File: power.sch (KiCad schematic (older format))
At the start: 34 parts, among them U1 TPS54325, U2 TPS54294

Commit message: Fix all the things
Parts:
- U1: symbol psu-components:TPS54325 -> Effect-Box-rescue:TPS54325-psu-components
- U2: symbol psu-components:TPS54294 -> Effect-Box-rescue:TPS54294-psu-components
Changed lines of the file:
@@
 $EndDescr
 $Comp
-L psu-components:TPS54325 U1
+L Effect-Box-rescue:TPS54325-psu-components U1
 U 1 1 5D81CBD0
 P 5700 2300
@@
 $EndComp
 $Comp
-L psu-components:TPS54294 U2
+L Effect-Box-rescue:TPS54294-psu-components U2
 U 1 1 5D821E10
 P 5750 4850

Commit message: Add PSU lib footprints
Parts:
- U1: symbol Effect-Box-rescue:TPS54325-psu-components -> Effect-Box-rescue:TPS54325
- U2: symbol Effect-Box-rescue:TPS54294-psu-components -> Effect-Box-rescue:TPS54294
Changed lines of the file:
@@
 $EndDescr
 $Comp
-L Effect-Box-rescue:TPS54325-psu-components U1
+L Effect-Box-rescue:TPS54325 U1
 U 1 1 5D81CBD0
 P 5700 2300
@@
 $EndComp
 $Comp
-L Effect-Box-rescue:TPS54294-psu-components U2
+L Effect-Box-rescue:TPS54294 U2
 U 1 1 5D821E10
 P 5750 4850

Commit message: Add footprints for real (such pain)
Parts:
- U1: footprint (none) -> Package_SO:TSSOP-14-1EP_4.4x5mm_P0.65mm
- U2: footprint (none) -> Package_SO:TSSOP-16-1EP_4.4x5mm_P0.65mm
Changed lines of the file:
@@
 F 0 "U1" H 5400 2700 50  0000 C CNN
 F 1 "TPS54325" H 5900 2700 50  0000 C CNN
-F 2 "" H 5700 2300 50  0001 C CNN
+F 2 "Package_SO:TSSOP-14-1EP_4.4x5mm_P0.65mm" H 5700 2300 50  0001 C CNN
 F 3 "" H 5700 2300 50  0001 C CNN
 	1    5700 2300
@@
 F 0 "U2" H 5450 5300 50  0000 C CNN
 F 1 "TPS54294" H 5950 5300 50  0000 C CNN
-F 2 "" H 5750 4850 50  0001 C CNN
+F 2 "Package_SO:TSSOP-16-1EP_4.4x5mm_P0.65mm" H 5750 4850 50  0001 C CNN
 F 3 "" H 5750 4850 50  0001 C CNN
 	1    5750 4850

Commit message: Export PSU components as libs
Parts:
- U1: symbol Effect-Box-rescue:TPS54325 -> tps54325:TPS54325
- U2: symbol Effect-Box-rescue:TPS54294 -> tps54294:TPS54294
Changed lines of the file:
@@
 $EndDescr
 $Comp
-L Effect-Box-rescue:TPS54325 U1
+L tps54325:TPS54325 U1
 U 1 1 5D81CBD0
 P 5700 2300
+AR Path="/5D81CBD0" Ref="U1"  Part="1"
+AR Path="/5D7D4441/5D81CBD0" Ref="U1"  Part="1"
 F 0 "U1" H 5400 2700 50  0000 C CNN
 F 1 "TPS54325" H 5900 2700 50  0000 C CNN
@@
 $EndComp
 $Comp
-L Effect-Box-rescue:TPS54294 U2
+L tps54294:TPS54294 U2
 U 1 1 5D821E10
 P 5750 4850
+AR Path="/5D821E10" Ref="U2"  Part="1"
+AR Path="/5D7D4441/5D821E10" Ref="U2"  Part="1"
 F 0 "U2" H 5450 5300 50  0000 C CNN
 F 1 "TPS54294" H 5950 5300 50  0000 C CNN

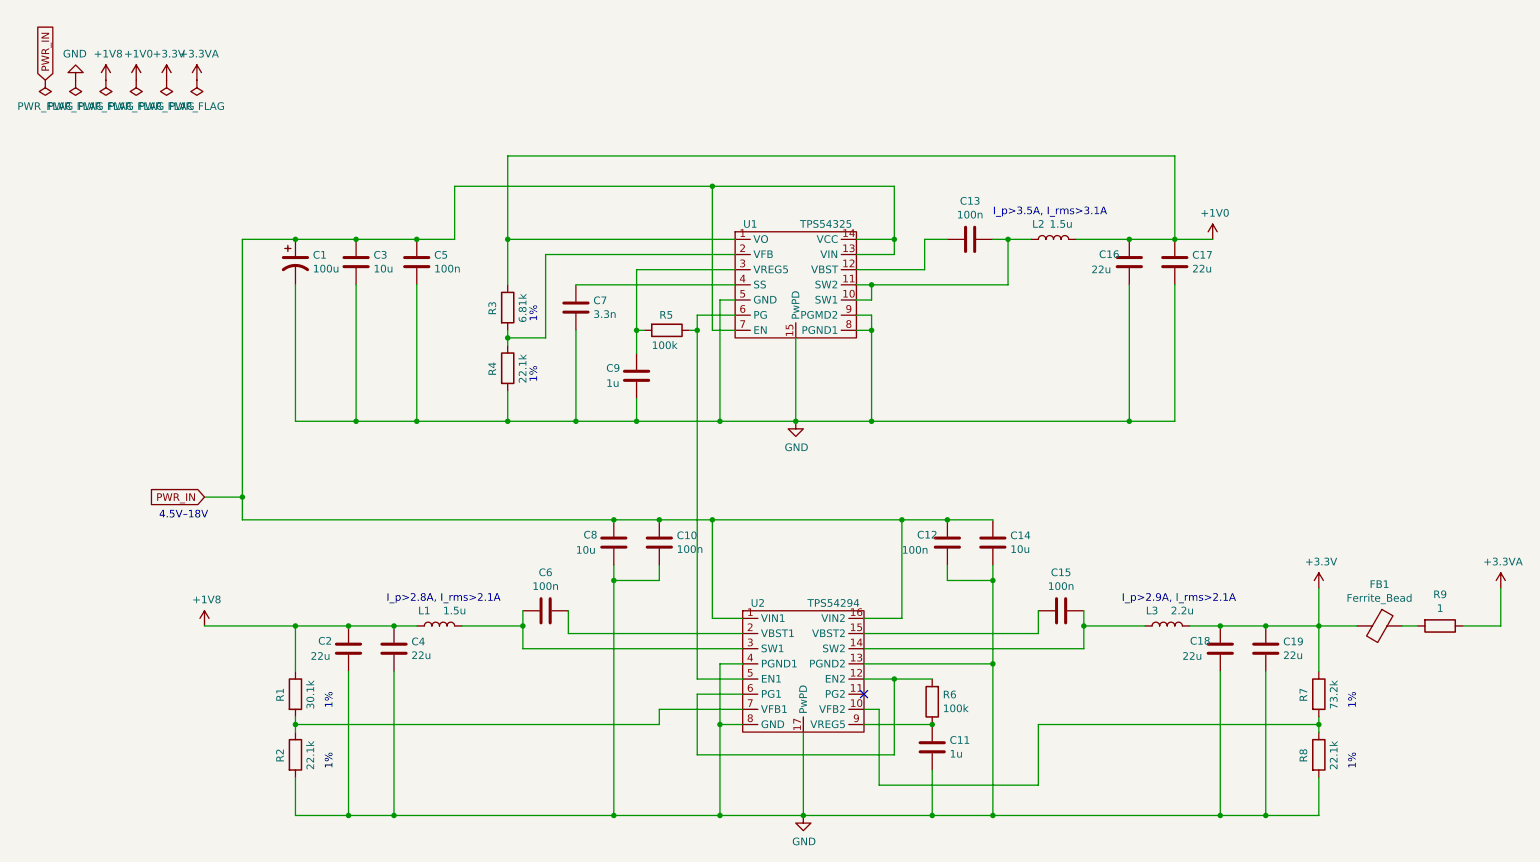
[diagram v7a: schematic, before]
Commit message: Change PSU
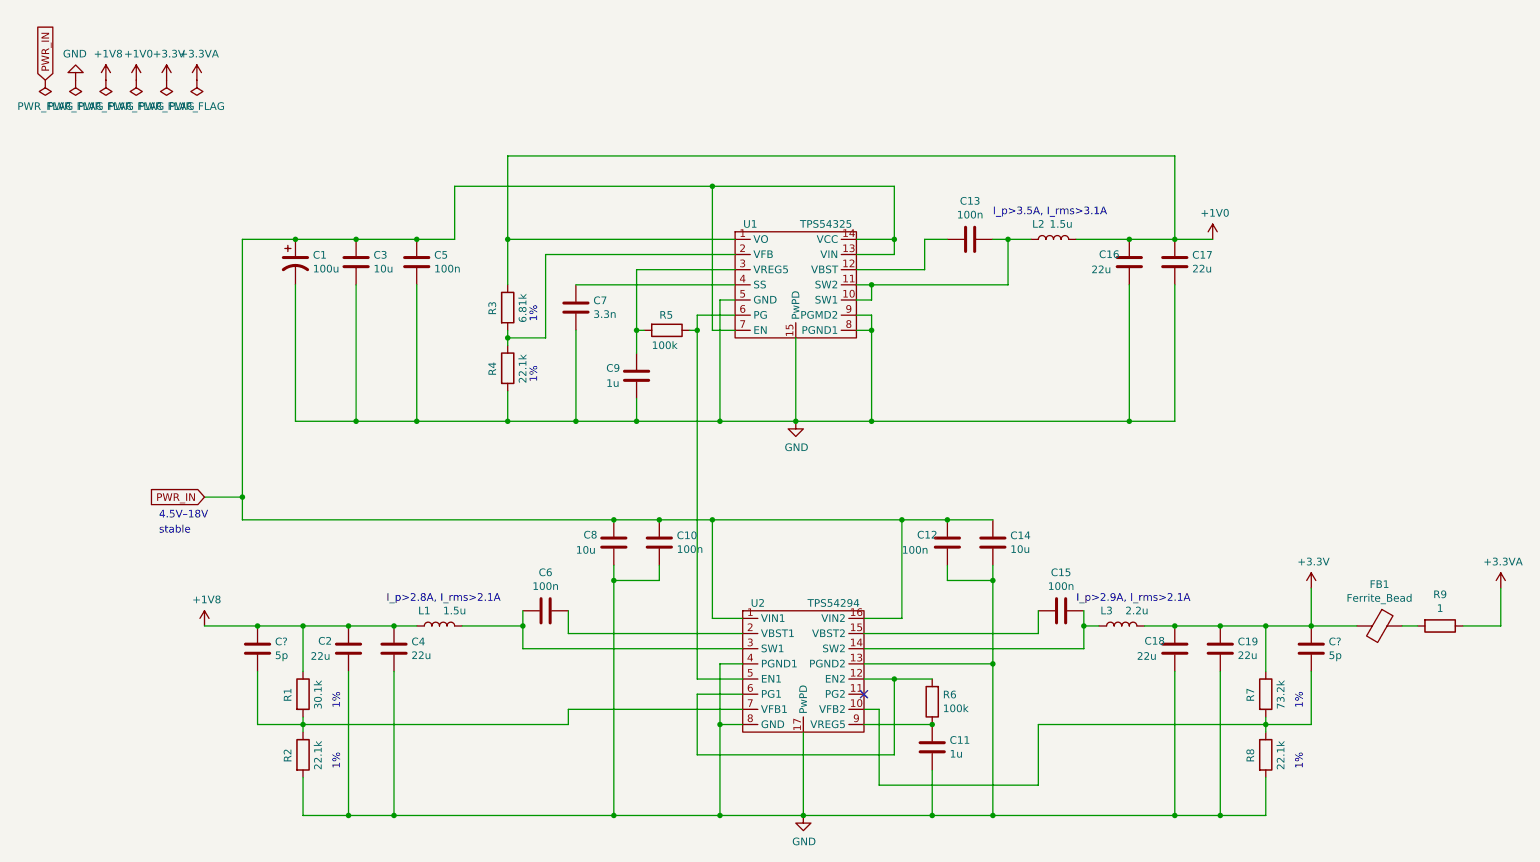
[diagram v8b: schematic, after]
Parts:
- added C? (x2): 5p, symbol Device:C
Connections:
- net +1V8: now also C?.1
- net +3V3: now also C?.1
- net at R7.2, R8.1, U2.10 (VFB2): now also C?.2
- net at R1.2, R2.1, U2.7 (VFB1): now also C?.2
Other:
- note added: "stable"
- moved on the sheet: C18, C19, L3, R1, R2, R7, R8
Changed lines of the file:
@@
 EESchema Schematic File Version 4
-LIBS:Effect-Box-cache
+LIBS:power-cache
 EELAYER 30 0
 EELAYER END
 $Descr A4 11693 8268
 encoding utf-8
-Sheet 5 5
+Sheet 1 1
 Title "Power supply unit"
 Date ""
@@
 L power:+3.3V #PWR05
 U 1 1 5D8254FC
-P 9150 4300
-F 0 "#PWR05" H 9150 4150 50  0001 C CNN
-F 1 "+3.3V" H 9165 4473 50  0000 C CNN
-F 2 "" H 9150 4300 50  0001 C CNN
-F 3 "" H 9150 4300 50  0001 C CNN
-	1    9150 4300
+P 9100 4300
+F 0 "#PWR05" H 9100 4150 50  0001 C CNN
+F 1 "+3.3V" H 9115 4473 50  0000 C CNN
+F 2 "" H 9100 4300 50  0001 C CNN
+F 3 "" H 9100 4300 50  0001 C CNN
+	1    9100 4300
 	1    0    0    -1
 $EndComp
@@
 L Device:R R1
 U 1 1 5D8B8984
-P 2400 5000
-F 0 "R1" V 2300 4950 50  0000 L CNN
-F 1 "30.1k" V 2500 4900 50  0000 L CNN
-F 2 "" V 2330 5000 50  0001 C CNN
-F 3 "~" H 2400 5000 50  0001 C CNN
-	1    2400 5000
-	1    0    0    -1
-$EndComp
-Text Notes 2650 5100 1    50   ~ 0
+P 2450 5000
+F 0 "R1" V 2350 4950 50  0000 L CNN
+F 1 "30.1k" V 2550 4900 50  0000 L CNN
+F 2 "" V 2380 5000 50  0001 C CNN
+F 3 "~" H 2450 5000 50  0001 C CNN
+	1    2450 5000
+	1    0    0    -1
+$EndComp
+Text Notes 2700 5100 1    50   ~ 0
 1%
-Text Notes 2650 5500 1    50   ~ 0
+Text Notes 2700 5500 1    50   ~ 0
 1%
 Wire Wire Line
 	2750 4550 3050 4550
-Connection ~ 2750 4550
 Wire Wire Line
 	3050 4550 3200 4550
 Connection ~ 3050 4550
 Wire Wire Line
-	2400 4850 2400 4550
+	2450 4850 2450 4550
 Wire Wire Line
 	6350 5400 6350 4900
@@
 Wire Wire Line
 	3900 4700 3900 4550
-Connection ~ 2400 5200
-Wire Wire Line
-	2400 5200 2400 5150
-Wire Wire Line
-	2400 5200 2400 5250
-Wire Wire Line
-	2400 5550 2400 5800
+Wire Wire Line
+	2450 5550 2450 5800
 $Comp
 L Device:R R2
 U 1 1 5D8B96AE
-P 2400 5400
-F 0 "R2" V 2300 5350 50  0000 L CNN
-F 1 "22.1k" V 2500 5300 50  0000 L CNN
-F 2 "" V 2330 5400 50  0001 C CNN
-F 3 "~" H 2400 5400 50  0001 C CNN
-	1    2400 5400
-	1    0    0    -1
-$EndComp
-Wire Wire Line
-	4800 5200 4800 5100
-Wire Wire Line
-	4800 5100 5350 5100
-Wire Wire Line
-	2400 5200 4800 5200
+P 2450 5400
+F 0 "R2" V 2350 5350 50  0000 L CNN
+F 1 "22.1k" V 2550 5300 50  0000 L CNN
+F 2 "" V 2380 5400 50  0001 C CNN
+F 3 "~" H 2450 5400 50  0001 C CNN
+	1    2450 5400
+	1    0    0    -1
+$EndComp
 Wire Wire Line
 	3500 4550 3900 4550
@@
 Wire Wire Line
 	3900 4550 3900 4450
-Wire Wire Line
-	2400 5800 2750 5800
-Connection ~ 2750 5800
 Wire Wire Line
 	3050 5800 2750 5800
@@
 Wire Wire Line
 	6150 4700 7600 4700
-Wire Wire Line
-	7600 4700 7600 4550
 $Comp
 L Device:L L3
 U 1 1 5D9B7D8B
-P 8150 4550
-F 0 "L3" V 8250 4650 50  0000 C CNN
-F 1 "2.2u" V 8250 4450 50  0000 C CNN
-F 2 "" H 8150 4550 50  0001 C CNN
-F 3 "~" H 8150 4550 50  0001 C CNN
-	1    8150 4550
+P 7850 4550
+F 0 "L3" V 7950 4650 50  0000 C CNN
+F 1 "2.2u" V 7950 4450 50  0000 C CNN
+F 2 "" H 7850 4550 50  0001 C CNN
+F 3 "~" H 7850 4550 50  0001 C CNN
+	1    7850 4550
 	0    -1   -1   0
 $EndComp
-Text Notes 7850 4400 0    50   ~ 0
+Text Notes 7550 4400 0    50   ~ 0
 I_p>2.9A, I_rms>2.1A
-Wire Wire Line
-	8000 4550 7600 4550
-Connection ~ 7600 4550
-Wire Wire Line
-	7600 4550 7600 4450
 $Comp
 L Device:C C19
 U 1 1 5D9C02F1
-P 8800 4700
-F 0 "C19" H 8915 4746 50  0000 L CNN
-F 1 "22u" H 8915 4655 50  0000 L CNN
-F 2 "" H 8838 4550 50  0001 C CNN
-F 3 "~" H 8800 4700 50  0001 C CNN
-	1    8800 4700
-	1    0    0    -1
-$EndComp
-$Comp
-L Device:C C18
-U 1 1 5D9C199F
 P 8500 4700
-F 0 "C18" H 8300 4750 50  0000 L CNN
-F 1 "22u" H 8250 4650 50  0000 L CNN
+F 0 "C19" H 8615 4746 50  0000 L CNN
+F 1 "22u" H 8615 4655 50  0000 L CNN
 F 2 "" H 8538 4550 50  0001 C CNN
 F 3 "~" H 8500 4700 50  0001 C CNN
@@
 	1    0    0    -1
 $EndComp
-Wire Wire Line
-	8300 4550 8500 4550
-Wire Wire Line
-	8800 4550 8500 4550
-Connection ~ 8500 4550
+$Comp
+L Device:C C18
+U 1 1 5D9C199F
+P 8200 4700
+F 0 "C18" H 8000 4750 50  0000 L CNN
+F 1 "22u" H 7950 4650 50  0000 L CNN
+F 2 "" H 8238 4550 50  0001 C CNN
+F 3 "~" H 8200 4700 50  0001 C CNN
+	1    8200 4700
+	1    0    0    -1
+$EndComp
+Wire Wire Line
+	8000 4550 8200 4550
+Wire Wire Line
+	8500 4550 8200 4550
+Connection ~ 8200 4550
+Wire Wire Line
+	8200 4850 8200 5800
 Wire Wire Line
 	8500 4850 8500 5800
 Wire Wire Line
-	8500 5800 7000 5800
-Connection ~ 7000 5800
-Wire Wire Line
-	8800 4850 8800 5800
-Wire Wire Line
-	8800 5800 8500 5800
-Connection ~ 8500 5800
+	8500 5800 8200 5800
 $Comp
 L Device:R R8
 U 1 1 5D9DCC5F
-P 9150 5400
-F 0 "R8" V 9050 5350 50  0000 L CNN
-F 1 "22.1k" V 9250 5300 50  0000 L CNN
-F 2 "" V 9080 5400 50  0001 C CNN
-F 3 "~" H 9150 5400 50  0001 C CNN
-	1    9150 5400
+P 8800 5400
+F 0 "R8" V 8700 5350 50  0000 L CNN
+F 1 "22.1k" V 8900 5300 50  0000 L CNN
+F 2 "" V 8730 5400 50  0001 C CNN
+F 3 "~" H 8800 5400 50  0001 C CNN
+	1    8800 5400
 	1    0    0    -1
 $EndComp
@@
 L Device:R R7
 U 1 1 5D9DE0E6
-P 9150 5000
-F 0 "R7" V 9050 4950 50  0000 L CNN
-F 1 "73.2k" V 9250 4900 50  0000 L CNN
-F 2 "" V 9080 5000 50  0001 C CNN
-F 3 "~" H 9150 5000 50  0001 C CNN
-	1    9150 5000
-	1    0    0    -1
-$EndComp
-Text Notes 9400 5100 1    50   ~ 0
+P 8800 5000
+F 0 "R7" V 8700 4950 50  0000 L CNN
+F 1 "73.2k" V 8900 4900 50  0000 L CNN
+F 2 "" V 8730 5000 50  0001 C CNN
+F 3 "~" H 8800 5000 50  0001 C CNN
+	1    8800 5000
+	1    0    0    -1
+$EndComp
+Text Notes 9050 5100 1    50   ~ 0
 1%
-Text Notes 9400 5500 1    50   ~ 0
+Text Notes 9050 5500 1    50   ~ 0
 1%
 Wire Wire Line
-	9150 5550 9150 5800
-Wire Wire Line
-	9150 5800 8800 5800
-Connection ~ 8800 5800
-Wire Wire Line
-	9150 5250 9150 5200
-Wire Wire Line
-	9150 4850 9150 4550
-Wire Wire Line
-	9150 4550 8800 4550
-Connection ~ 8800 4550
-Wire Wire Line
-	9150 4550 9150 4300
-Connection ~ 9150 4550
+	8800 5550 8800 5800
 Wire Wire Line
 	6150 5100 6250 5100
@@
 Wire Wire Line
 	7300 5600 7300 5200
-Wire Wire Line
-	7300 5200 9150 5200
-Connection ~ 9150 5200
-Wire Wire Line
-	9150 5200 9150 5150
 NoConn ~ 6150 5000
 Wire Wire Line
@@
 $EndComp
 Wire Wire Line
-	9150 4550 9400 4550
-Wire Wire Line
 	9700 4550 9800 4550
 Wire Wire Line
@@
 Wire Wire Line
 	10350 4550 10350 4300
-Wire Wire Line
-	1800 4550 2400 4550
-Connection ~ 2400 4550
-Wire Wire Line
-	2400 4550 2750 4550
 Wire Wire Line
 	6600 5800 5750 5800
@@
 	1    0    0    -1
 $EndComp
+Wire Wire Line
+	7600 4450 7600 4550
+Wire Wire Line
+	7000 5800 8200 5800
+Connection ~ 7000 5800
+Connection ~ 8200 5800
+Wire Wire Line
+	7700 4550 7600 4550
+Connection ~ 7600 4550
+Wire Wire Line
+	7600 4550 7600 4700
+$Comp
+L Device:C C?
+U 1 1 5D8E4A98
+P 9100 4700
+F 0 "C?" H 9215 4746 50  0000 L CNN
+F 1 "5p" H 9215 4655 50  0000 L CNN
+F 2 "" H 9138 4550 50  0001 C CNN
+F 3 "~" H 9100 4700 50  0001 C CNN
+	1    9100 4700
+	1    0    0    -1
+$EndComp
+Wire Wire Line
+	8800 5150 8800 5200
+Wire Wire Line
+	9400 4550 9100 4550
+Wire Wire Line
+	9100 4550 8800 4550
+Connection ~ 9100 4550
+Connection ~ 8500 4550
+Wire Wire Line
+	8800 4850 8800 4550
+Connection ~ 8800 4550
+Wire Wire Line
+	8800 4550 8500 4550
+Wire Wire Line
+	8800 5200 9100 5200
+Wire Wire Line
+	9100 5200 9100 4850
+Connection ~ 8800 5200
+Wire Wire Line
+	8800 5200 8800 5250
+Wire Wire Line
+	8800 5200 7300 5200
+Wire Wire Line
+	8500 5800 8800 5800
+Connection ~ 8500 5800
+Wire Wire Line
+	9100 4550 9100 4300
+$Comp
+L Device:C C?
+U 1 1 5D943CC4
+P 2150 4700
+F 0 "C?" H 2265 4746 50  0000 L CNN
+F 1 "5p" H 2265 4655 50  0000 L CNN
+F 2 "" H 2188 4550 50  0001 C CNN
+F 3 "~" H 2150 4700 50  0001 C CNN
+	1    2150 4700
+	1    0    0    -1
+$EndComp
+Wire Wire Line
+	2450 5150 2450 5200
+Connection ~ 2450 5200
+Wire Wire Line
+	2450 5200 2450 5250
+Wire Wire Line
+	2450 5200 2150 5200
+Wire Wire Line
+	2150 5200 2150 4850
+Wire Wire Line
+	2750 5800 2450 5800
+Connection ~ 2750 5800
+Wire Wire Line
+	2750 4550 2450 4550
+Connection ~ 2750 4550
+Wire Wire Line
+	2450 4550 2150 4550
+Connection ~ 2450 4550
+Wire Wire Line
+	2150 4550 1800 4550
+Connection ~ 2150 4550
+Text Notes 1500 3950 0    50   ~ 0
+stable
+Wire Wire Line
+	4200 5100 4200 5200
+Wire Wire Line
+	4200 5200 2450 5200
+Wire Wire Line
+	4200 5100 5350 5100
 $EndSCHEMATC
